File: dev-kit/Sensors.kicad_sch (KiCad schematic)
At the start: 16 parts, among them IC201 APDS-9306-065, IC202 BMI270, IC203 BMP581, IC204 LIS2MDLTR, Q201 DMG1013UW-7

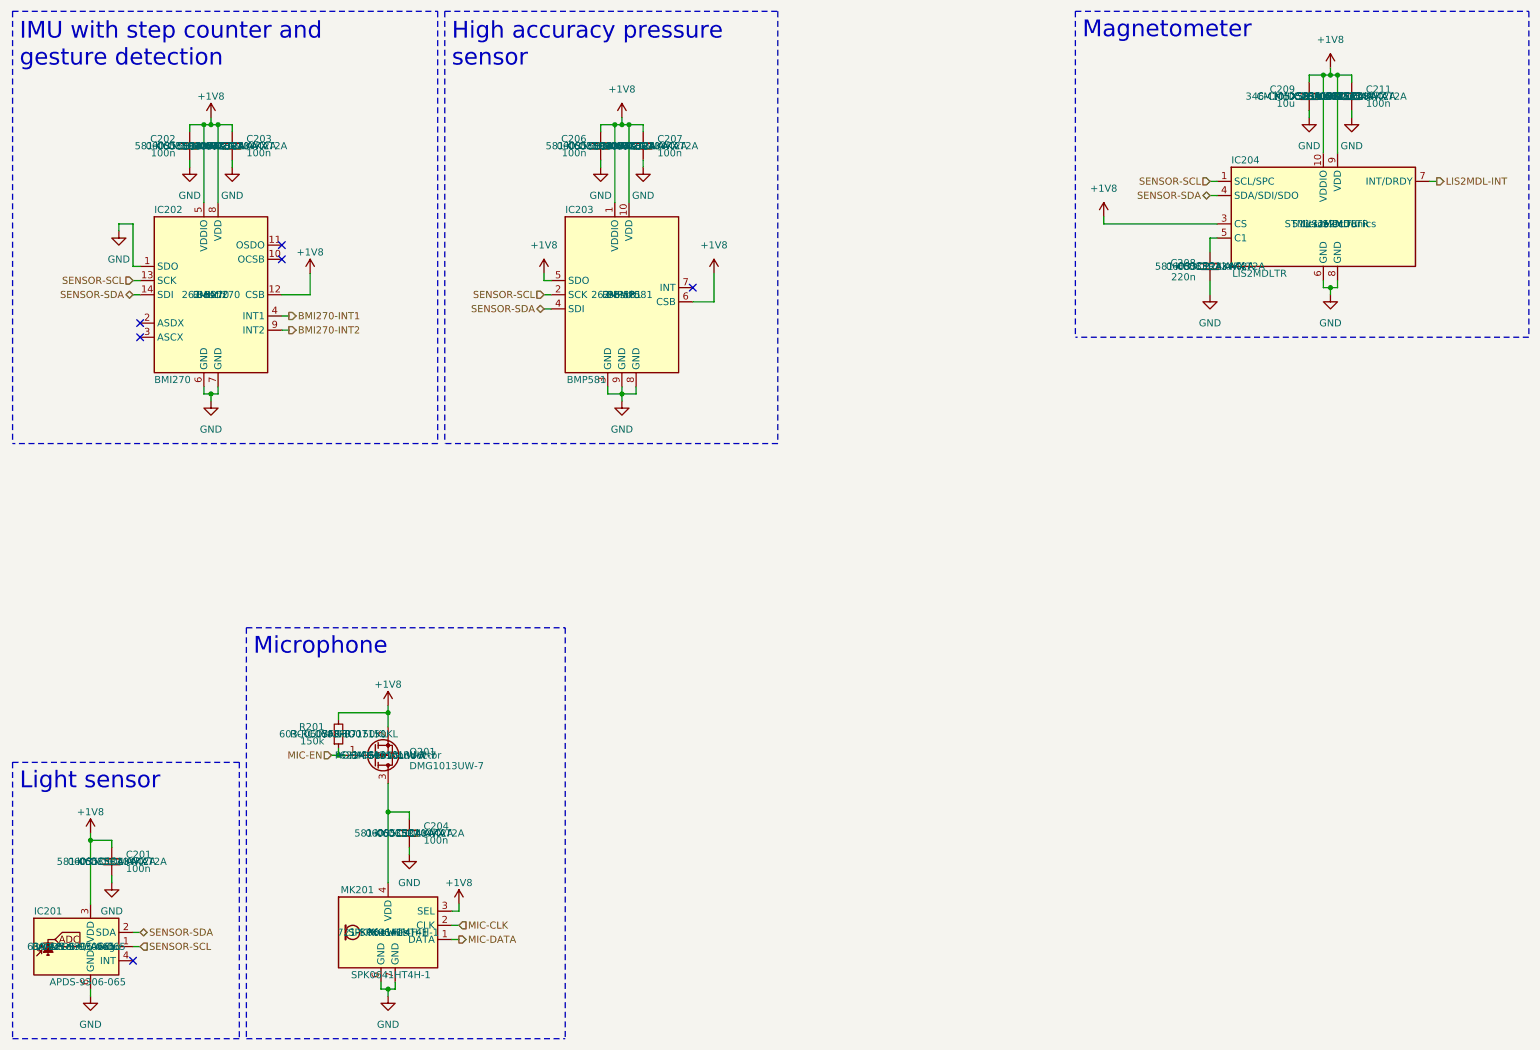
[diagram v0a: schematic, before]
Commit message: PCB: Add new vibration motor
- Remove old hardware project (comes back later)
- Add new dev-kit project

Closes #102

Signed-off-by: Daniel Kampert <danielkampert@kampis-elektroecke.de>
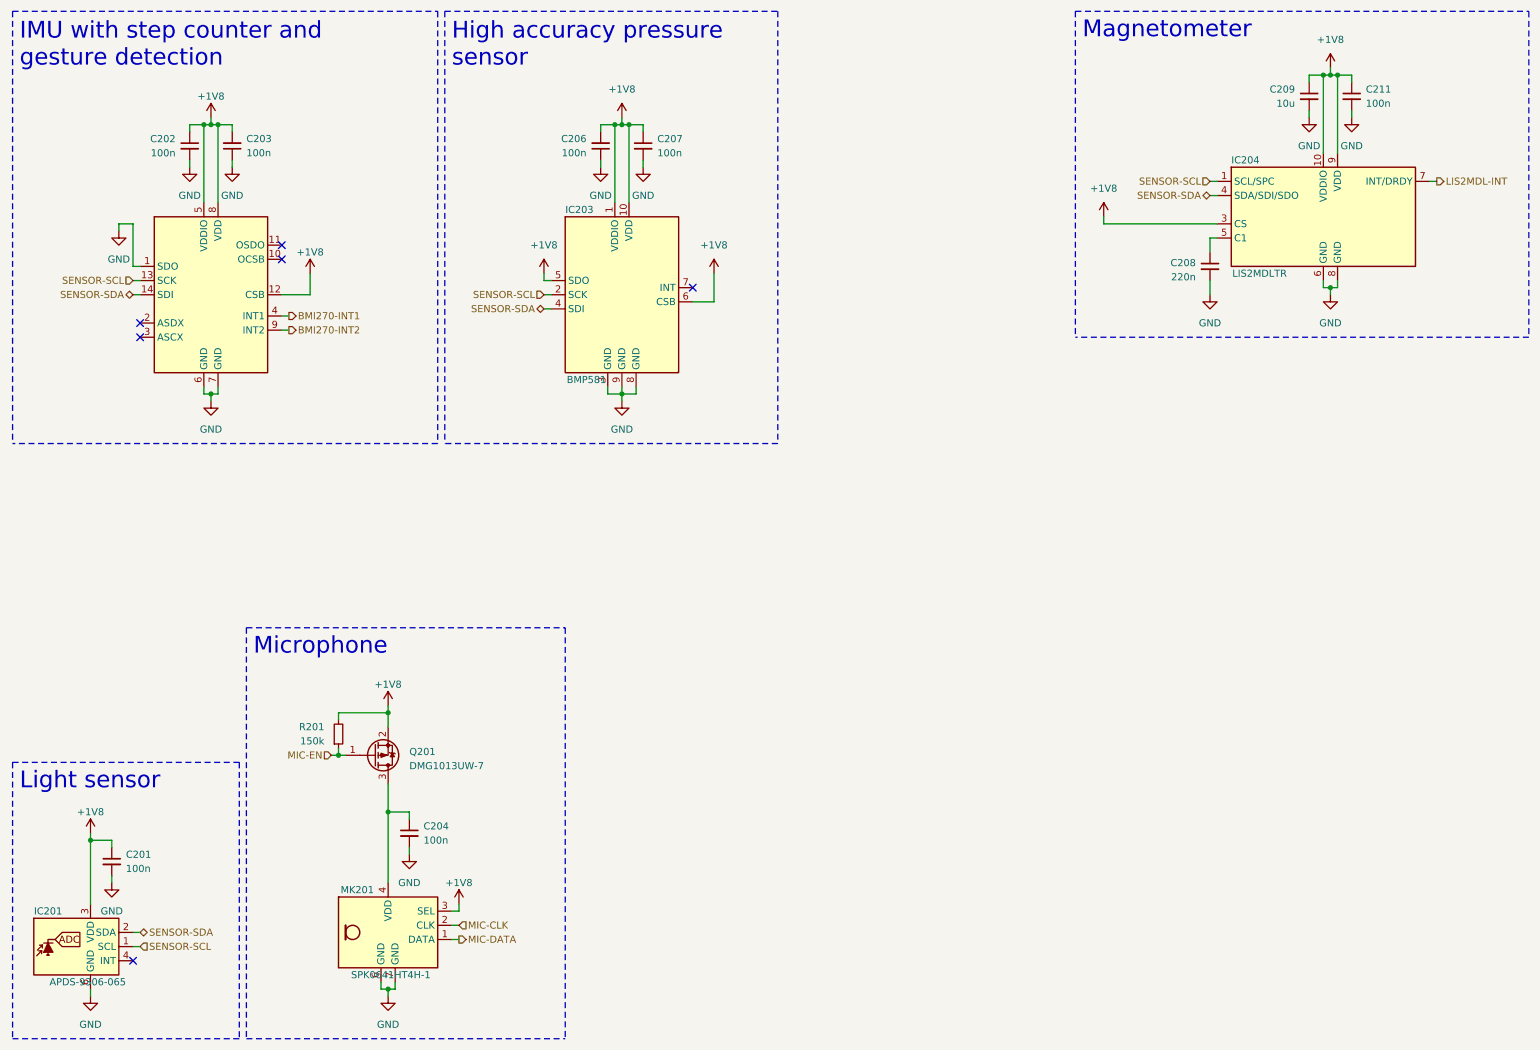
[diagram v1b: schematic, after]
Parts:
- C201, C202, C203, C204, C206, C207, C208, C209, C211, IC201, IC202, IC203, IC204, MK201, Q201, R201: Distributor Mouser -> (none)
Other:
- title: ZSWatch v3 -> ZSWatch v3 Dev-Kit
